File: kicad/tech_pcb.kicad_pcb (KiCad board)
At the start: 2 copper layers, 18.3 x 31.7 mm, 24 parts, among them J1 Conn_01x10, J2 Conn_01x10, J3 USB_C_Receptacle_USB2.0_16P, J4 Conn_01x03_MountingPin, SW1 SW_Push, SW2 SW_Push, U1 STM32C071GBUxN, U2 XC6206PxxxMR

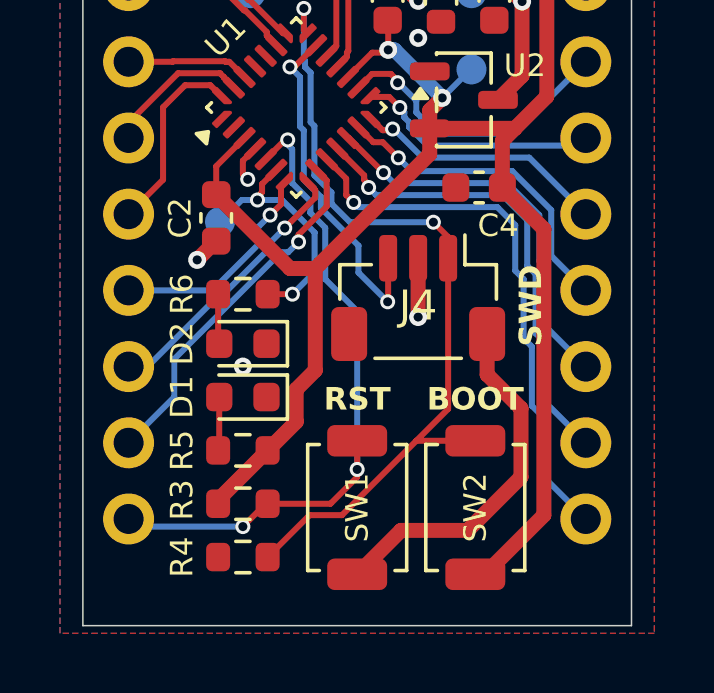
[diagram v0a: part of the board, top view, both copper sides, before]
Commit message: Update part selections and add BOM
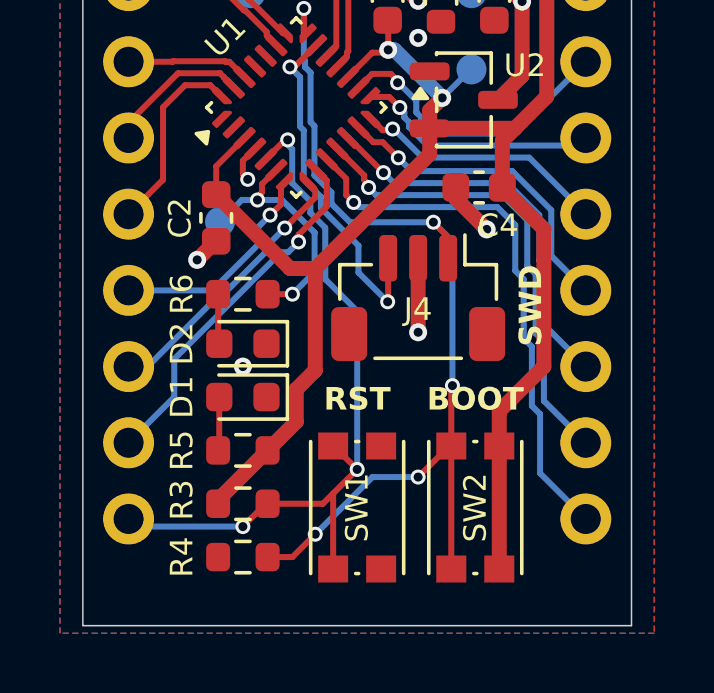
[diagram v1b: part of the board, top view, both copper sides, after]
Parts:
- SW1, SW2: footprint Button_Switch_SMD:SW_SPST_TS-1088-xR025 -> Button_Switch_SMD:SW_Push_1P1T_NO_CK_KMR2
- turned SW1 to -90 degrees
- turned SW2 to 90 degrees
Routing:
- net GND: track 23.4 -> 13.7 mm, vias 6 -> 7
- net /BOOT0: track 27.9 -> 32.3 mm, vias 2 -> 5
- net /NRST: track 22.9 -> 25.5 mm
- net +3V3: track 58.0 -> 57.3 mm

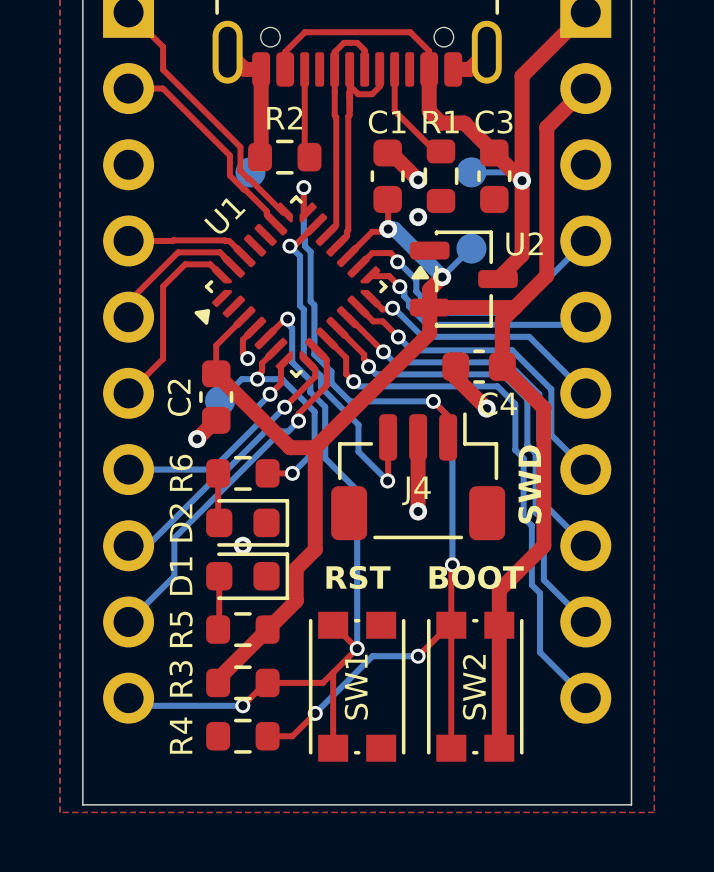
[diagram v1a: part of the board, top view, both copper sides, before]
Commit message: Fix via sizes for osh park
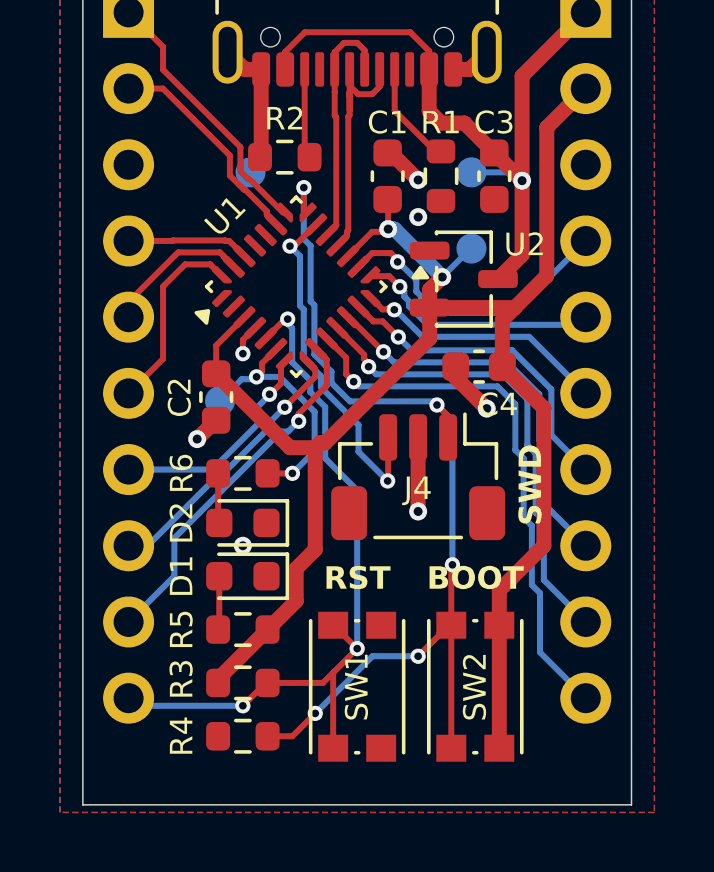
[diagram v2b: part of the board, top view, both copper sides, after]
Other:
- board text added: "TTU PCB Workshop Prototype v0.1"

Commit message: Update board to v0.2
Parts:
- C3, C4: footprint Capacitor_SMD:C_0603_1608Metric -> Capacitor_SMD:C_0805_2012Metric
- D1, D2: footprint LED_SMD:LED_0603_1608Metric -> LED_SMD:LED_0805_2012Metric
- J1, J2: value Conn_01x10 -> Conn_01x11; footprint Connector_PinHeader_2.54mm:PinHeader_1x10_P2.54mm_Vertical -> Connector_PinHeader_2.54mm:PinHeader_1x11_P2.54mm_Vertical
- R3, R4, R5, R6: footprint Resistor_SMD:R_0603_1608Metric -> Resistor_SMD:R_0805_2012Metric
- SW1: value SW_Push -> RST
- SW2: value SW_Push -> BOOT
- moved J4 35.3 mm to (30.2, 33.4), turned to 90 degrees
- moved TP3 33.4 mm to (30.8, 29.8)
- moved SW2 32.3 mm to (31.0, 50.2), turned to 0 degrees
- moved C4 30.8 mm to (35.6, 33.0), turned to 90 degrees
- moved R4 28.4 mm to (29.8, 46.4)
- moved R1 28.3 mm to (35.6, 29.4)
- moved R2 28.2 mm to (30.5, 29.0)
- moved TP1 27.9 mm to (34.4, 40.4)
- moved J1 27.5 mm to (25.4, 25.4)
- moved C3 27.5 mm to (38.6, 29.0), turned to 0 degrees
- moved R5 26.7 mm to (38.6, 35.6), turned to 0 degrees
- moved J3 26.7 mm to (34.3, 22.9)
- moved U2 26.3 mm to (39.0, 32.2)
- moved C2 25.5 mm to (28.6, 43.7)
- moved J2 25.2 mm to (43.2, 25.4)
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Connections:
- J1 pad 10: /NRST -> /PC14
- J1 pad 4: /PB6 -> /PB4
- J1 pad 5: /PB7 -> /PB5
- J1 pad 6: /PB8 -> /PB6
- J1 pad 7: /PA1 -> /PB7
- J1 pad 8: /PA2 -> /PB8
- J1 pad 9: /PA3 -> /PC15
- U1 pad 1: unconnected-(U1-PC14-Pad1) -> /PC15
- U1 pad 2: unconnected-(U1-PC15-Pad2) -> /PC14
- U1 pad 24: unconnected-(U1-PB4-Pad24) -> /PB4
- U1 pad 25: unconnected-(U1-PB5-Pad25) -> /PB5
- U1 pad 6: /STATUS -> unconnected-(U1-PA0-Pad6)
- U1 pad 7: /PA1 -> unconnected-(U1-PA1-Pad7)
- U1 pad 8: /PA2 -> /STATUS
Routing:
- net +3V3: track 57.4 -> 18.7 mm
- net +5V: track 23.9 -> 3.71 mm
- net /PA2: track 9.30 -> 0.00 mm, vias 1 -> 0
- net /PC14: track 0.00 -> 9.25 mm
- net /PB4: track 0.00 -> 8.69 mm
- net /PA1: track 7.44 -> 0.00 mm, vias 1 -> 0
- net /PA15: track 8.92 -> 16.0 mm
- net /PC15: track 0.00 -> 6.83 mm
- net /PB3: track 7.26 -> 13.6 mm
- net /PB5: track 0.00 -> 6.35 mm
- net /BOOT0: track 32.1 -> 26.2 mm, vias 5 -> 2
- net GND: track 13.4 -> 8.46 mm, vias 7 -> 8
- net /PA3: track 12.1 -> 16.8 mm, vias 1 -> 0
- net /USB_DP: track 7.96 -> 12.6 mm
- net /PA8: track 9.97 -> 14.5 mm, vias 1 -> 0
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- added copper zone on F.Cu, net +3V3
- added copper zone on F.Cu, net +5V
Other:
- board size 18.3 x 31.7 mm -> 22.4 x 34 mm
- board text added: "TN Tech PCB Workshop Prototype v0.2"
- board text removed: "SWD"
- board text removed: "TTU PCB Workshop Prototype v0.1"
